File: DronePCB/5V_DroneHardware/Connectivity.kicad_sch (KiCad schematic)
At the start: 8 parts, among them J301 USB_B_Micro, J302 BATTERY, J303 SWD_CONN, U301 USBLC6-2SC6

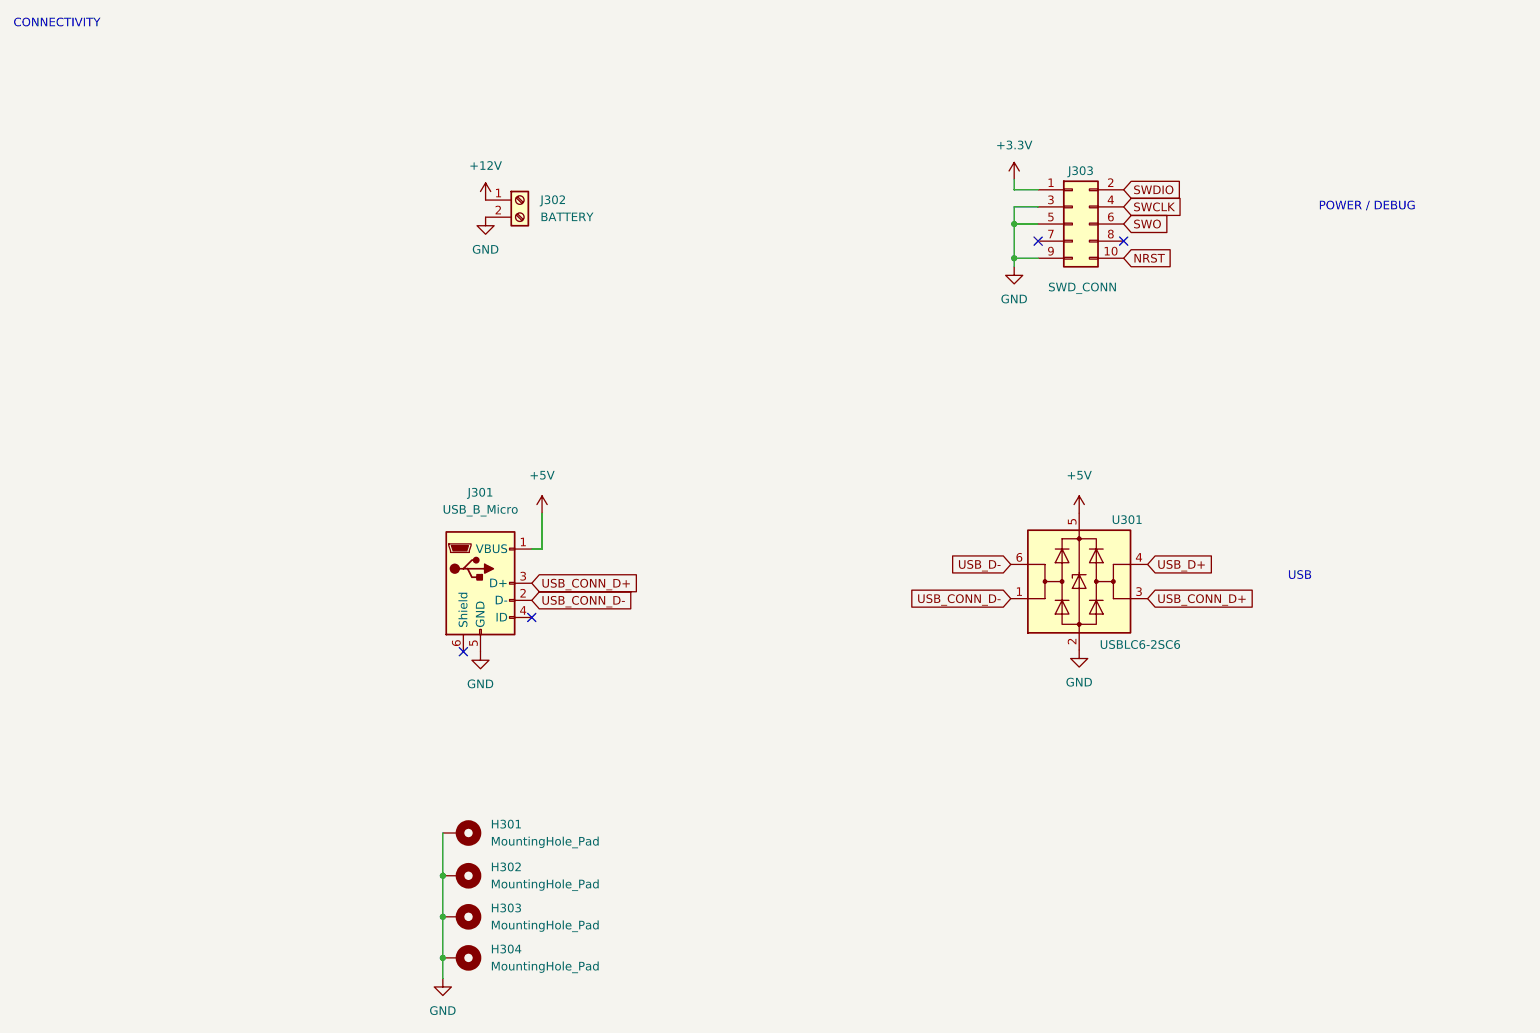
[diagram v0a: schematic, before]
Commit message: Collegamento di USB con resistenze da 22Ohm
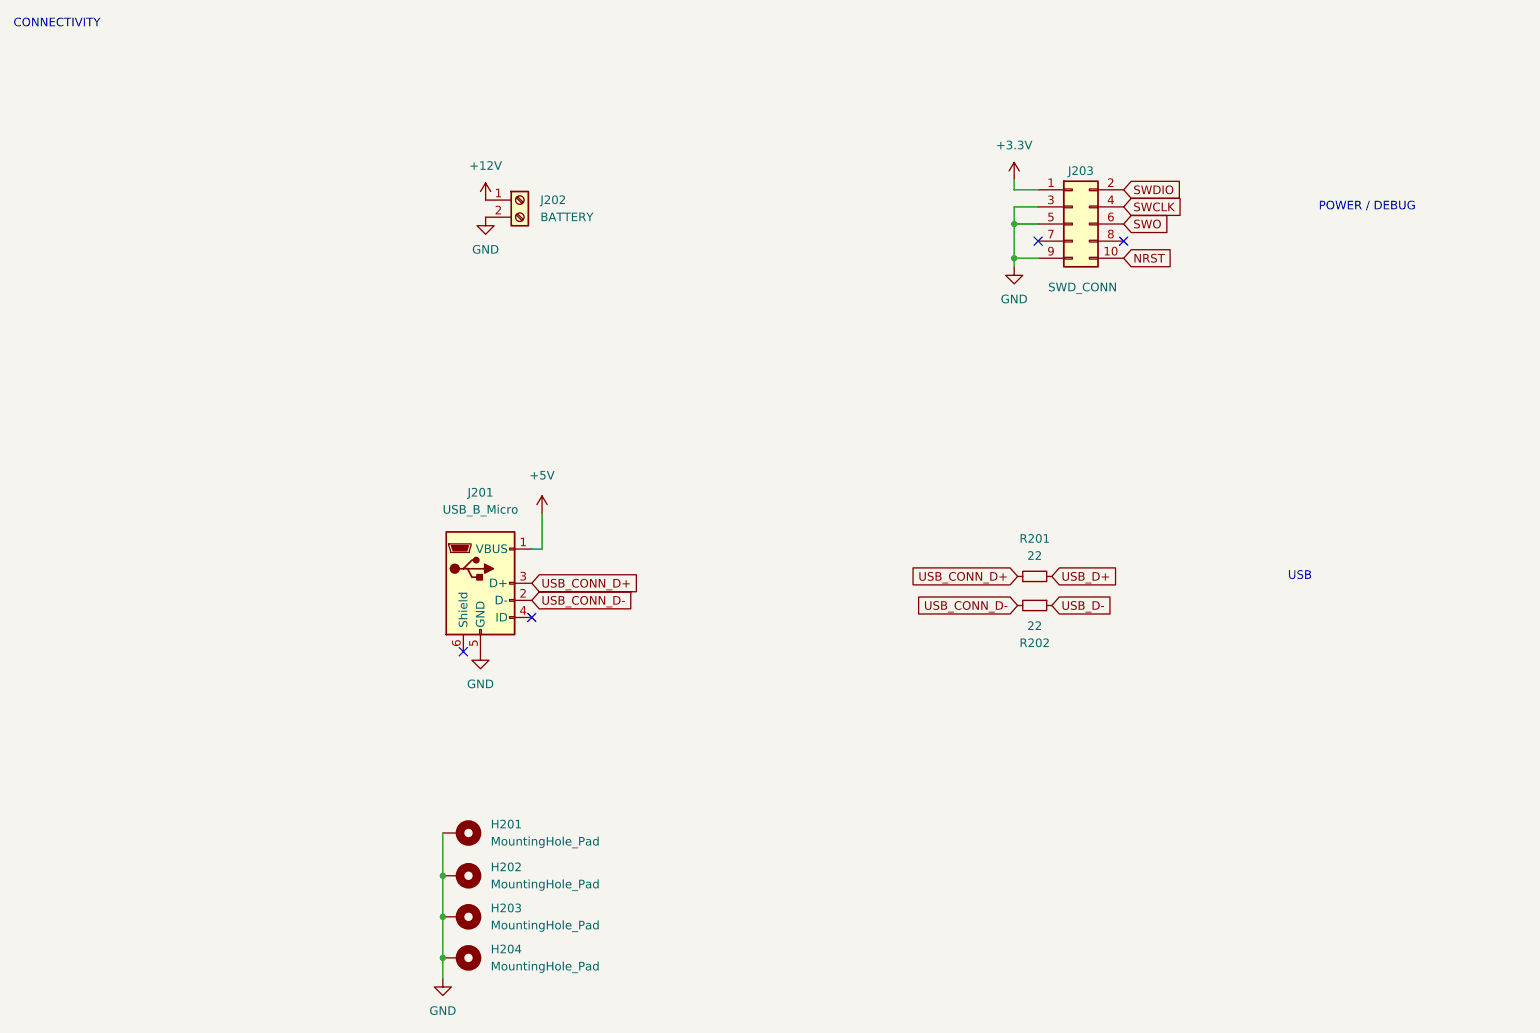
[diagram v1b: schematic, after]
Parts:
- removed U301: USBLC6-2SC6, Package_TO_SOT_SMD:SOT-23-6, symbol Power_Protection:USBLC6-2SC6
- added R201, R202: 22, Resistor_SMD:R_0201_0603Metric, symbol Device:R_Small
- renumbered H301 to H201, H302 to H202, H303 to H203, H304 to H204, J301 to J201, J302 to J202, J303 to J203
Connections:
- net USB_CONN_D+: now also R201.1
- net USB_CONN_D-: now also R202.2
- net USB_D+: now also R201.2
- net USB_D-: now also R202.1

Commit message: Collegamento di dei segnali PWM dei motori
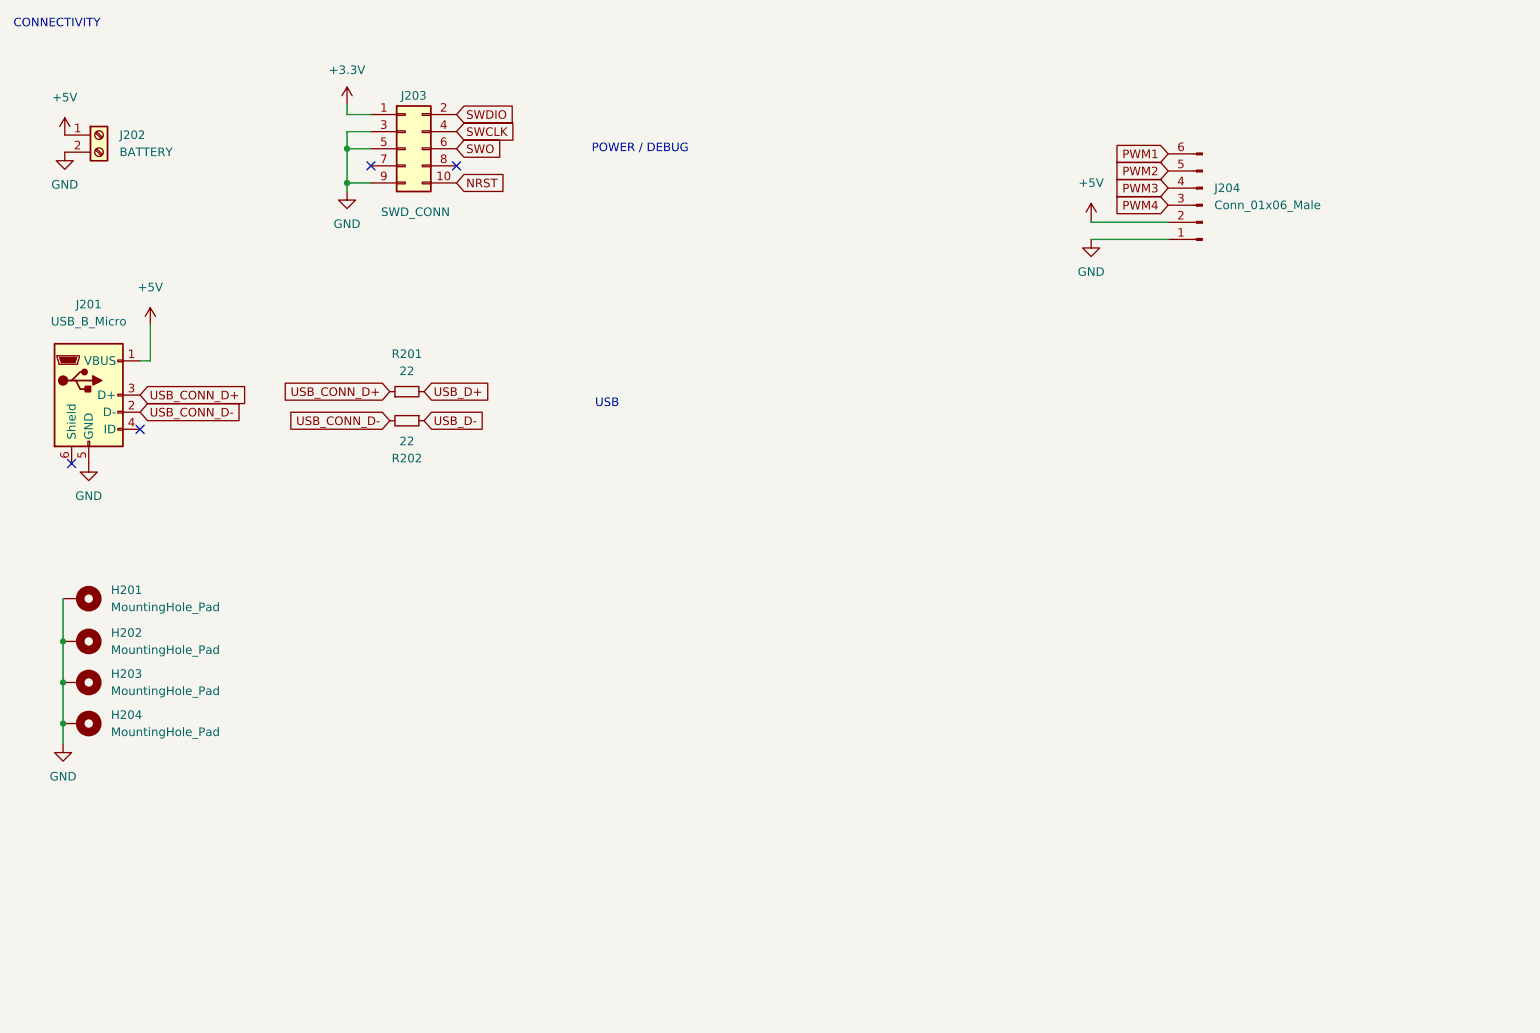
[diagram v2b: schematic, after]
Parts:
- added J204: Conn_01x06_Male, Connector_Hirose:Hirose_DF52-6S-0.8H_1x06-1MP_P0.80mm_Horizontal, symbol Connector:Conn_01x06_Male
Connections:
- net +12V is gone; now on net +5V: J202.1 (Pin_1)
- net +5V: now also J204.2 (Pin_2)
- net GND: now also J204.1 (Pin_1)
- new net PWM1: J204.6 (Pin_6)
- new net PWM2: J204.5 (Pin_5)
- new net PWM3: J204.4 (Pin_4)
- new net PWM4: J204.3 (Pin_3)
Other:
- moved on the sheet: H201, H202, H203, H204, J201, J202, J203, R201, R202

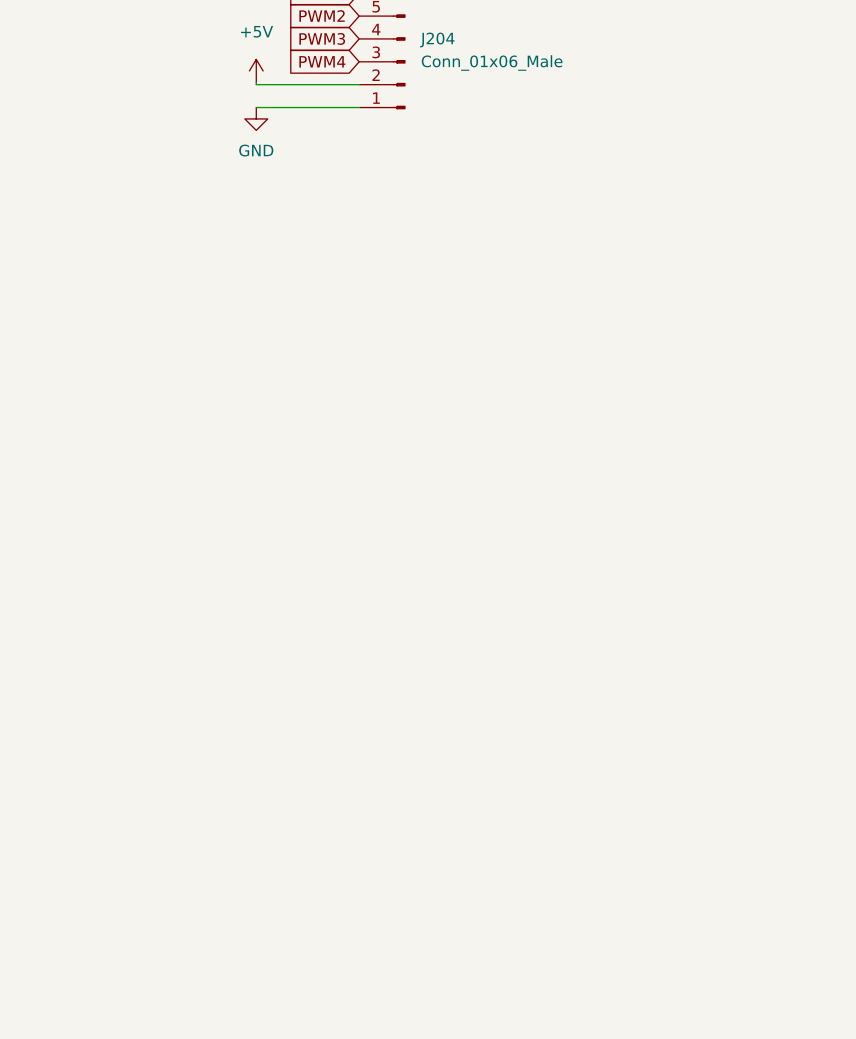
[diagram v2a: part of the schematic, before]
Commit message: Aggiunta di USART per RC
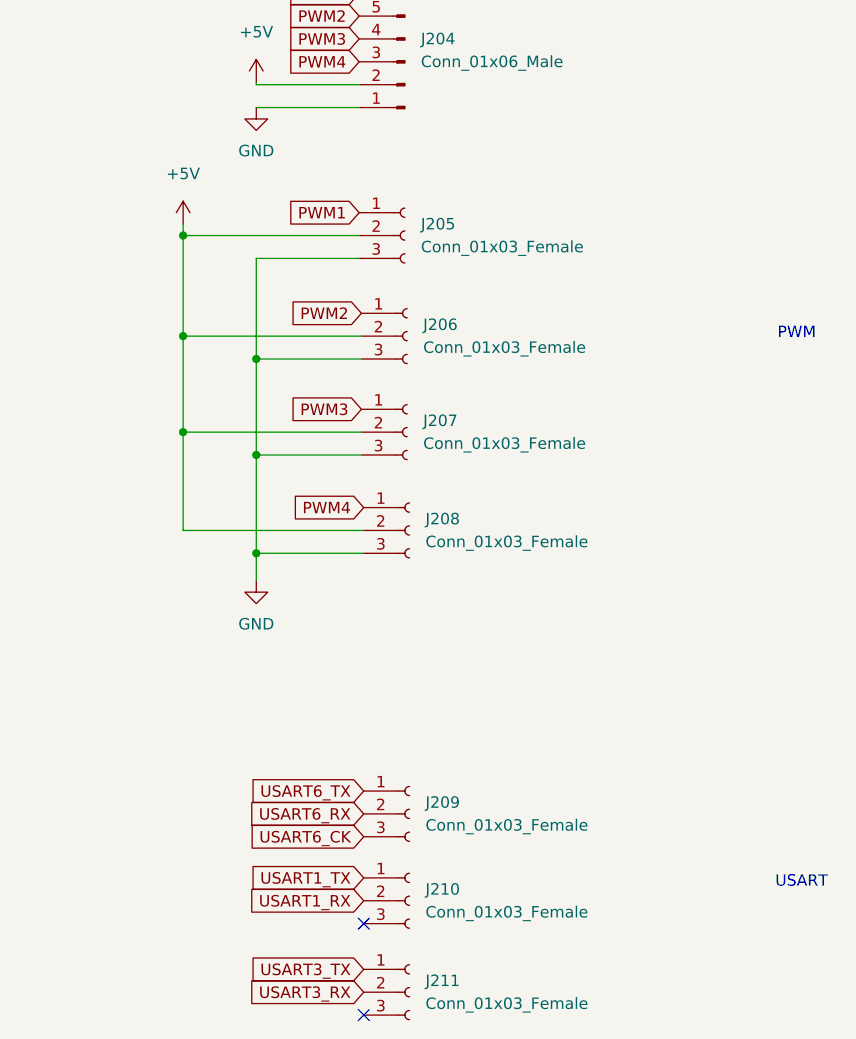
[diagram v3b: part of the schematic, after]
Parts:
- added J205, J206, J207, J208, J209, J210, J211: Conn_01x03_Female, Connector_PinHeader_1.00mm:PinHeader_1x03_P1.00mm_Vertical, symbol Connector:Conn_01x03_Female
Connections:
- net +5V: now also J205.2 (Pin_2), J206.2 (Pin_2), J207.2 (Pin_2), J208.2 (Pin_2)
- net GND: now also J205.3 (Pin_3), J206.3 (Pin_3), J207.3 (Pin_3), J208.3 (Pin_3)
- net PWM1: now also J205.1 (Pin_1)
- net PWM2: now also J206.1 (Pin_1)
- net PWM3: now also J207.1 (Pin_1)
- net PWM4: now also J208.1 (Pin_1)
- new net USART1_RX: J210.2 (Pin_2)
- new net USART1_TX: J210.1 (Pin_1)
- new net USART3_RX: J211.2 (Pin_2)
- new net USART3_TX: J211.1 (Pin_1)
- new net USART6_CK: J209.3 (Pin_3)
- new net USART6_RX: J209.2 (Pin_2)
- new net USART6_TX: J209.1 (Pin_1)
- no-connect marks 4 -> 6
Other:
- note added: "PWM"
- note added: "USART"

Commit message: BOM e pos file
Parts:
- R201, R202: LCSC Part # (none) -> C270355
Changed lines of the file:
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@@
+      (effects (font (size 1.27 1.27)) hide)
+    )
+    (property "LCSC Part #" "C270355" (id 4) (at 71.882 68.834 0)
       (effects (font (size 1.27 1.27)) hide)
     )
@@
       (effects (font (size 1.27 1.27)) hide)
     )
+    (property "LCSC Part #" "C270355" (id 4) (at 71.882 73.152 0)
+      (effects (font (size 1.27 1.27)) hide)
+    )

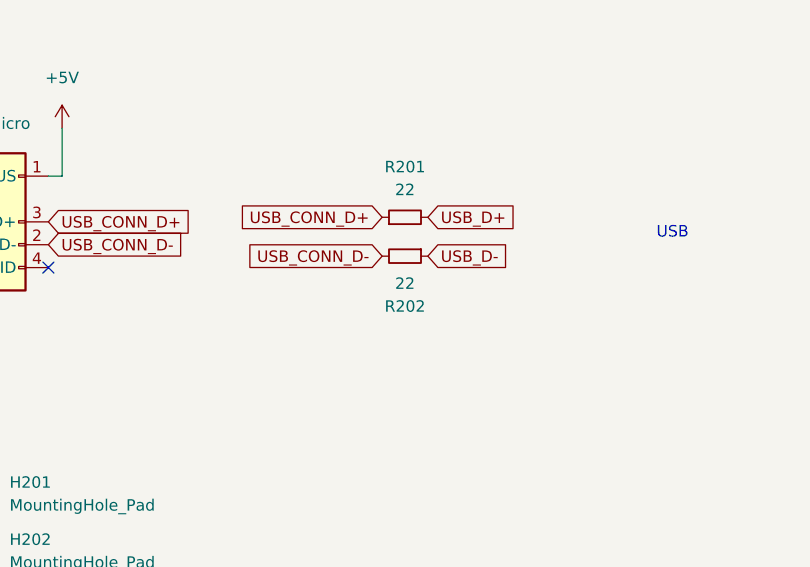
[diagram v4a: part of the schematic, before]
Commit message: Modifica delle componenti 0201 in componenti 0402
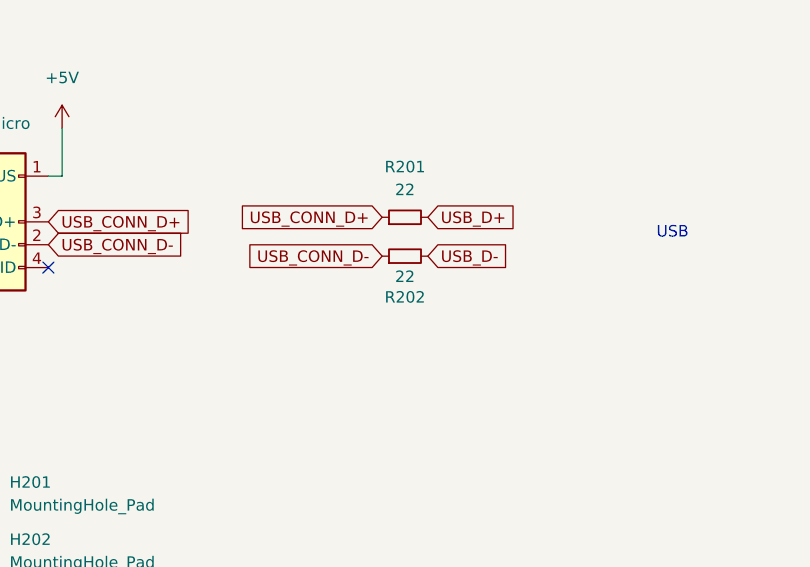
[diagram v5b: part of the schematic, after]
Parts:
- R201, R202: footprint Resistor_SMD:R_0201_0603Metric -> Resistor_SMD:R_0402_1005Metric; LCSC Part # C270355 -> C25092
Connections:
- net USB_CONN_D-: now also R202.1; no longer R202.2
- net USB_D-: now also R202.2; no longer R202.1
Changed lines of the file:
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@@
     (pin "1")
+  )
+  (symbol (lib_id "Device:R_Small") (at 71.882 73.152 90) (unit 1)
+    (in_bom yes) (on_board yes)
+    (property "Reference" "R202" (id 0) (at 71.882 77.724 90))
+    (property "Value" "22" (id 1) (at 71.882 75.438 90))
+    (property "Footprint" "Resistor_SMD:R_0402_1005Metric" (id 2) (at 71.882 73.152 0)
+      (effects (font (size 1.27 1.27)) hide)
+    )
+    (property "Datasheet" "~" (id 3) (at 71.882 73.152 0)
+      (effects (font (size 1.27 1.27)) hide)
+    )
+    (property "LCSC Part #" "C25092" (id 4) (at 71.882 73.152 0)
+      (effects (font (size 1.27 1.27)) hide)
+    )
+    (pin "1")
+    (pin "2")
   )
   (symbol (lib_id "Device:R_Small") (at 71.882 68.834 90) (unit 1)
@@
     (property "Reference" "R201" (id 0) (at 71.882 63.246 90))
     (property "Value" "22" (id 1) (at 71.882 65.786 90))
-    (property "Footprint" "Resistor_SMD:R_0201_0603Metric" (id 2) (at 71.882 68.834 0)
+    (property "Footprint" "Resistor_SMD:R_0402_1005Metric" (id 2) (at 71.882 68.834 0)
       (effects (font (size 1.27 1.27)) hide)
     )
@@
       (effects (font (size 1.27 1.27)) hide)
     )
-    (property "LCSC Part #" "C270355" (id 4) (at 71.882 68.834 0)
+    (property "LCSC Part #" "C25092" (id 4) (at 71.882 68.834 0)
       (effects (font (size 1.27 1.27)) hide)
     )
@@
     (pin "3")
   )
-  (symbol (lib_id "Device:R_Small") (at 71.882 73.152 270) (unit 1)
-    (in_bom yes) (on_board yes) (fields_autoplaced)
-    (property "Reference" "R202" (id 0) (at 71.882 78.74 90))
-    (property "Value" "22" (id 1) (at 71.882 76.2 90))
-    (property "Footprint" "Resistor_SMD:R_0201_0603Metric" (id 2) (at 71.882 73.152 0)
-      (effects (font (size 1.27 1.27)) hide)
-    )
-    (property "Datasheet" "~" (id 3) (at 71.882 73.152 0)
-      (effects (font (size 1.27 1.27)) hide)
-    )
-    (property "LCSC Part #" "C270355" (id 4) (at 71.882 73.152 0)
-      (effects (font (size 1.27 1.27)) hide)
-    )
-    (pin "1")
-    (pin "2")
-  )
   (symbol (lib_id "Connector:Conn_01x03_Female") (at 190.5 134.366 0) (unit 1)
